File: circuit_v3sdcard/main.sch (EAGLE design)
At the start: 20 parts, among them CN1 SD, CN3 MICROSD, CN4 5035481020, IC1 C8051F381-GM, IC3 N25Q512A, IC4 KC2016K, IC6 MPU-9250

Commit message: Modified parts values
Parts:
- D4: value HSMS-2854 -> BAT54CL
- IC3: value N25Q512A -> MT29F2G01ABAGDWB
- IC4: value KC2016K -> KC2016K48.0000C1GE00
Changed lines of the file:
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@@
 <part name="SUPPLY6" library="supply2" deviceset="DGND" device=""/>
 <part name="C6" library="reg,cap" deviceset="C-" device="1005" value="1.0u"/>
-<part name="IC3" library="EEPROM" deviceset="N25Q512A" device=""/>
+<part name="IC3" library="EEPROM" deviceset="N25Q512A" device="" value="MT29F2G01ABAGDWB"/>
 <part name="C9" library="reg,cap" deviceset="C-" device="1005" value="0.1u"/>
 <part name="+3V7" library="supply1" deviceset="+3V3" device=""/>
 <part name="SUPPLY13" library="supply2" deviceset="DGND" device=""/>
 <part name="SUPPLY14" library="supply2" deviceset="DGND" device=""/>
-<part name="IC4" library="Oscillator" deviceset="KC2016K" device=""/>
+<part name="IC4" library="Oscillator" deviceset="KC2016K" device="" value="KC2016K48.0000C1GE00"/>
 <part name="+3V8" library="supply1" deviceset="+3V3" device=""/>
 <part name="SUPPLY15" library="supply2" deviceset="DGND" device=""/>
@@
 <part name="SUPPLY3" library="supply2" deviceset="DGND" device=""/>
 <part name="SUPPLY1" library="supply2" deviceset="DGND" device=""/>
-<part name="D4" library="avago" library_urn="urn:adsk.eagle:library:107" deviceset="HSMS-2854" device="" package3d_urn="urn:adsk.eagle:package:4488/1"/>
+<part name="D4" library="avago" library_urn="urn:adsk.eagle:library:107" deviceset="HSMS-2854" device="" package3d_urn="urn:adsk.eagle:package:4488/1" value="BAT54CL"/>
 <part name="R3" library="reg,cap" deviceset="R-" device="1005" value="100"/>
 <part name="C1" library="reg,cap" deviceset="C-" device="1005" value="1.0u"/>

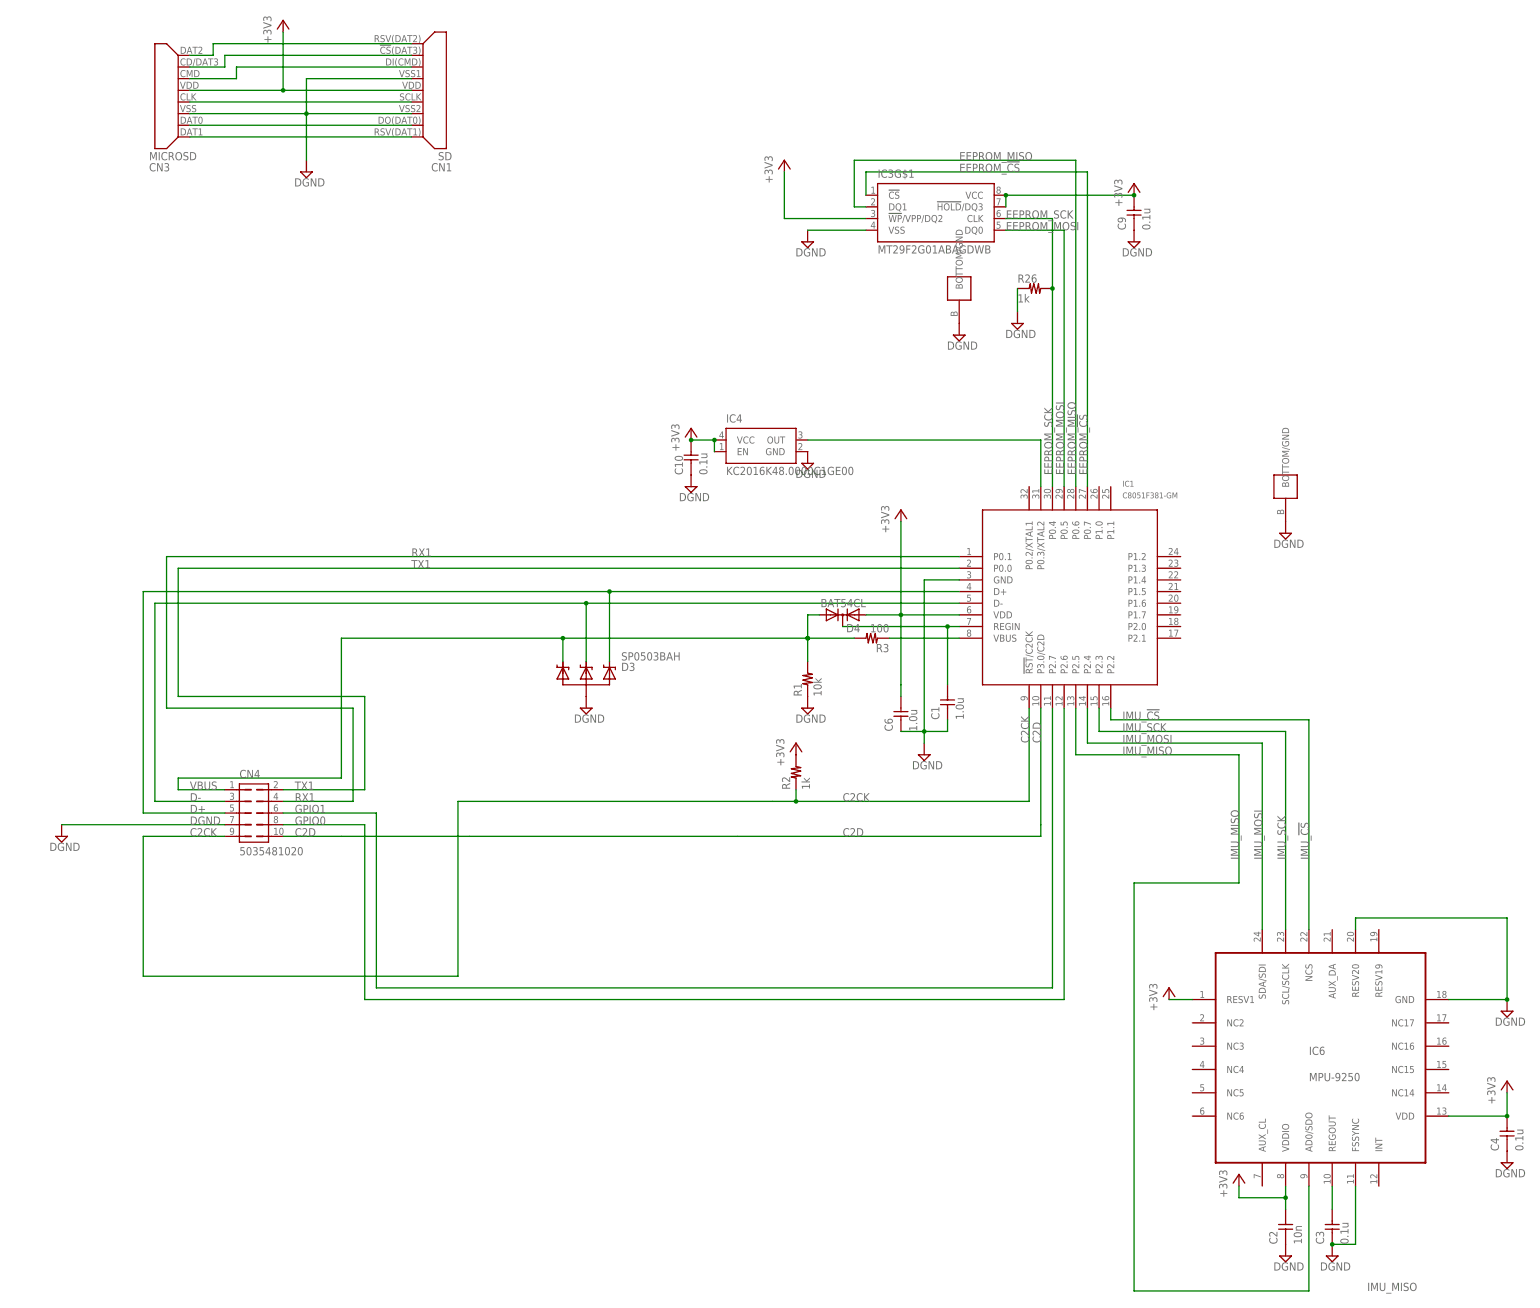
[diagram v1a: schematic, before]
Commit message: Modifing sdcard circuit
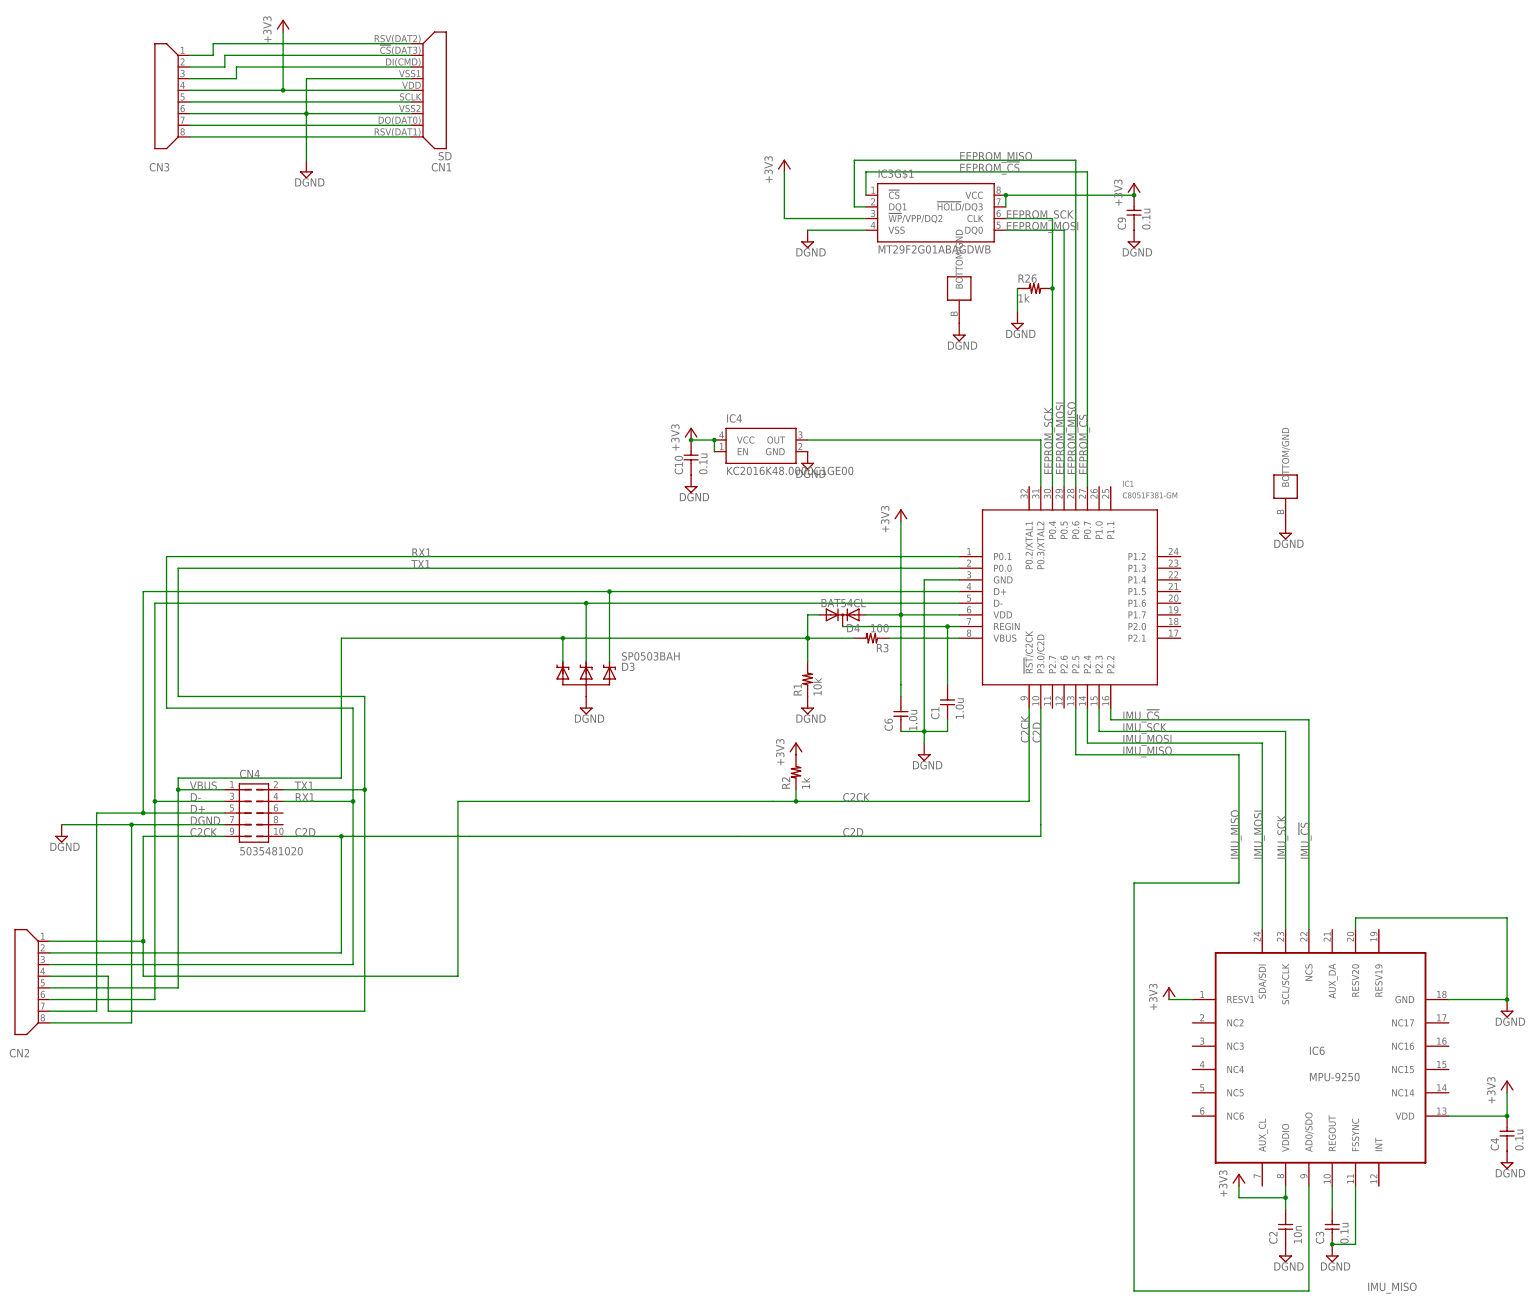
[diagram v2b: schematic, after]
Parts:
- added CN2: (no value), Connector:MICROSD
- CN3: value MICROSD -> (none)
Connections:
- removed net GPIO0: CN4.8, IC1G$1.P2.6
- removed net GPIO1: CN4.6, IC1G$1.P2.7
- net C2CK: now also CN2.P$1
- net C2D: now also CN2.P$2
- net D+: now also CN2.P$7
- net D-: now also CN2.P$6
- net DGND: now also CN2.P$8
- net RX1: now also CN2.P$3
- net TX1: now also CN2.P$4
- net VBUS: now also CN2.P$5
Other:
- moved on the sheet: CN3
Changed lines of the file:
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@@
 <?xml version="1.0" encoding="utf-8"?>
 <!DOCTYPE eagle SYSTEM "eagle.dtd">
-<eagle version="9.2.0">
+<eagle version="9.1.3">
 <drawing>
 <settings>
@@
 <part name="R3" library="reg,cap" deviceset="R-" device="1005" value="100"/>
 <part name="C1" library="reg,cap" deviceset="C-" device="1005" value="1.0u"/>
+<part name="CN2" library="Connector" deviceset="MICROSD" device=""/>
 </parts>
 <sheets>
@@
 <attribute name="NAME" x="-27.178" y="-25.4" size="1.778" layer="95" rot="R90"/>
 <attribute name="VALUE" x="-21.844" y="-25.4" size="1.778" layer="96" rot="R90"/>
+</instance>
+<instance part="CN2" gate="G$1" x="-226.06" y="-83.82">
+<attribute name="NAME" x="-229.87" y="-98.933" size="1.778" layer="95"/>
+<attribute name="VALUE" x="-229.87" y="-96.52" size="1.778" layer="96"/>
 </instance>
 </instances>
@@
 <label x="-190.5" y="-48.26" size="1.778" layer="95"/>
 <pinref part="CN4" gate="G$1" pin="7"/>
-<wire x1="-182.88" y1="-48.26" x2="-218.44" y2="-48.26" width="0.1524" layer="91"/>
+<wire x1="-182.88" y1="-48.26" x2="-203.2" y2="-48.26" width="0.1524" layer="91"/>
+<pinref part="CN2" gate="G$1" pin="P$8"/>
+<wire x1="-203.2" y1="-48.26" x2="-218.44" y2="-48.26" width="0.1524" layer="91"/>
+<wire x1="-203.2" y1="-48.26" x2="-203.2" y2="-91.44" width="0.1524" layer="91"/>
+<wire x1="-203.2" y1="-91.44" x2="-220.98" y2="-91.44" width="0.1524" layer="91"/>
+<junction x="-203.2" y="-48.26"/>
 </segment>
 </net>
@@
 <wire x1="-132.08" y1="-43.18" x2="-132.08" y2="-81.28" width="0.1524" layer="91"/>
 <wire x1="-132.08" y1="-81.28" x2="-200.66" y2="-81.28" width="0.1524" layer="91"/>
-<wire x1="-200.66" y1="-81.28" x2="-200.66" y2="-50.8" width="0.1524" layer="91"/>
+<wire x1="-200.66" y1="-81.28" x2="-200.66" y2="-73.66" width="0.1524" layer="91"/>
 <pinref part="CN4" gate="G$1" pin="9"/>
+<wire x1="-200.66" y1="-73.66" x2="-200.66" y2="-50.8" width="0.1524" layer="91"/>
 <wire x1="-200.66" y1="-50.8" x2="-182.88" y2="-50.8" width="0.1524" layer="91"/>
 <label x="-190.5" y="-50.8" size="1.778" layer="95"/>
+<pinref part="CN2" gate="G$1" pin="P$1"/>
+<wire x1="-200.66" y1="-73.66" x2="-220.98" y2="-73.66" width="0.1524" layer="91"/>
+<junction x="-200.66" y="-73.66"/>
 </segment>
 </net>
@@
 <wire x1="-157.48" y1="-50.8" x2="-170.18" y2="-50.8" width="0.1524" layer="91"/>
 <label x="-167.64" y="-50.8" size="1.778" layer="95"/>
+<pinref part="CN2" gate="G$1" pin="P$2"/>
+<wire x1="-157.48" y1="-50.8" x2="-157.48" y2="-76.2" width="0.1524" layer="91"/>
+<wire x1="-157.48" y1="-76.2" x2="-220.98" y2="-76.2" width="0.1524" layer="91"/>
+<junction x="-157.48" y="-50.8"/>
 </segment>
 </net>
@@
 <pinref part="CN4" gate="G$1" pin="3"/>
 <wire x1="-198.12" y1="-43.18" x2="-182.88" y2="-43.18" width="0.1524" layer="91"/>
+<pinref part="CN2" gate="G$1" pin="P$6"/>
+<wire x1="-198.12" y1="-43.18" x2="-198.12" y2="-86.36" width="0.1524" layer="91"/>
+<wire x1="-198.12" y1="-86.36" x2="-220.98" y2="-86.36" width="0.1524" layer="91"/>
+<junction x="-198.12" y="-43.18"/>
 </segment>
 </net>
@@
 <pinref part="CN4" gate="G$1" pin="5"/>
 <wire x1="-200.66" y1="-45.72" x2="-182.88" y2="-45.72" width="0.1524" layer="91"/>
+<wire x1="-200.66" y1="-45.72" x2="-210.82" y2="-45.72" width="0.1524" layer="91"/>
+<junction x="-200.66" y="-45.72"/>
+<wire x1="-210.82" y1="-45.72" x2="-210.82" y2="-88.9" width="0.1524" layer="91"/>
+<pinref part="CN2" gate="G$1" pin="P$7"/>
+<wire x1="-210.82" y1="-88.9" x2="-220.98" y2="-88.9" width="0.1524" layer="91"/>
 </segment>
 </net>
@@
 <wire x1="-182.88" y1="-40.64" x2="-193.04" y2="-40.64" width="0.1524" layer="91"/>
 <wire x1="-193.04" y1="-40.64" x2="-193.04" y2="-38.1" width="0.1524" layer="91"/>
+<pinref part="CN2" gate="G$1" pin="P$5"/>
+<wire x1="-193.04" y1="-40.64" x2="-193.04" y2="-83.82" width="0.1524" layer="91"/>
+<wire x1="-193.04" y1="-83.82" x2="-220.98" y2="-83.82" width="0.1524" layer="91"/>
+<junction x="-193.04" y="-40.64"/>
 </segment>
 </net>
@@
 <pinref part="CN4" gate="G$1" pin="4"/>
 <wire x1="-154.94" y1="-43.18" x2="-170.18" y2="-43.18" width="0.1524" layer="91"/>
+<pinref part="CN2" gate="G$1" pin="P$3"/>
+<wire x1="-154.94" y1="-43.18" x2="-154.94" y2="-78.74" width="0.1524" layer="91"/>
+<wire x1="-154.94" y1="-78.74" x2="-220.98" y2="-78.74" width="0.1524" layer="91"/>
+<junction x="-154.94" y="-43.18"/>
 </segment>
 </net>
@@
 <pinref part="CN4" gate="G$1" pin="2"/>
 <wire x1="-170.18" y1="-40.64" x2="-152.4" y2="-40.64" width="0.1524" layer="91"/>
-</segment>
-</net>
-<net name="GPIO0" class="0">
-<segment>
-<label x="-167.64" y="-48.26" size="1.778" layer="95"/>
-<pinref part="IC1" gate="G$1" pin="P2.6"/>
-<wire x1="0" y1="-22.86" x2="0" y2="-86.36" width="0.1524" layer="91"/>
-<wire x1="0" y1="-86.36" x2="-152.4" y2="-86.36" width="0.1524" layer="91"/>
-<wire x1="-152.4" y1="-86.36" x2="-152.4" y2="-48.26" width="0.1524" layer="91"/>
-<pinref part="CN4" gate="G$1" pin="8"/>
-<wire x1="-170.18" y1="-48.26" x2="-152.4" y2="-48.26" width="0.1524" layer="91"/>
-</segment>
-</net>
-<net name="GPIO1" class="0">
-<segment>
-<label x="-167.64" y="-45.72" size="1.778" layer="95"/>
-<pinref part="IC1" gate="G$1" pin="P2.7"/>
-<wire x1="-149.86" y1="-83.82" x2="-2.54" y2="-83.82" width="0.1524" layer="91"/>
-<wire x1="-2.54" y1="-83.82" x2="-2.54" y2="-22.86" width="0.1524" layer="91"/>
-<wire x1="-149.86" y1="-83.82" x2="-149.86" y2="-45.72" width="0.1524" layer="91"/>
-<pinref part="CN4" gate="G$1" pin="6"/>
-<wire x1="-170.18" y1="-45.72" x2="-149.86" y2="-45.72" width="0.1524" layer="91"/>
-</segment>
-</net>
+<wire x1="-152.4" y1="-40.64" x2="-152.4" y2="-88.9" width="0.1524" layer="91"/>
+<wire x1="-152.4" y1="-88.9" x2="-208.28" y2="-88.9" width="0.1524" layer="91"/>
+<junction x="-152.4" y="-40.64"/>
+<wire x1="-208.28" y1="-88.9" x2="-208.28" y2="-81.28" width="0.1524" layer="91"/>
+<pinref part="CN2" gate="G$1" pin="P$4"/>
+<wire x1="-208.28" y1="-81.28" x2="-220.98" y2="-81.28" width="0.1524" layer="91"/>
+</segment>
+</net>

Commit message: Modified circuit
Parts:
- removed CN4: 5035481020, Connector:5035481020
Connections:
- net +3V3: now also IC6G$1.RESV1, IC6G$1.VDD, IC6G$1.VDDIO; no longer IC6.RESV1, IC6.VDD, IC6.VDDIO
- net C2CK: no longer CN4.9
- net C2D: no longer CN4.10
- net D+: no longer CN4.5
- net D-: no longer CN4.3
- net DGND: now also IC6G$1.FSSYNC, IC6G$1.GND, IC6G$1.RESV20, IC6G$2.BOTTOM/GND; no longer CN4.7, IC6.FSSYNC, IC6.GND, IC6.RESV20
- net IMU_!CS: now also IC6G$1.NCS; no longer IC6.NCS
- net IMU_MISO: now also IC6G$1.AD0/SDO; no longer IC6.AD0/SDO
- net IMU_MOSI: now also IC6G$1.SDA/SDI; no longer IC6.SDA/SDI
- net IMU_SCK: now also IC6G$1.SCL/SCLK; no longer IC6.SCL/SCLK
- net N$13: now also IC6G$1.REGOUT; no longer IC6.REGOUT
- net RX1: no longer CN4.4
- net TX1: no longer CN4.2
- net VBUS: no longer CN4.1
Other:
- moved on the sheet: R2
